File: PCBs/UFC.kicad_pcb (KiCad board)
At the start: 2 copper layers, 63 parts, among them J3 Power, J5 Matrix, J7 Driver output 2, J9 Driver output 1, SW1 SW_SPST, SW10 SW_SPST, SW11 SW_SPST, SW12 SW_SPST, SW13 SW_SPST, SW14 SW_SPST, SW15 SW_SPST, SW16 SW_SPST, SW17 SW_SPST, SW2 SW_SPST, SW3 SW_SPST, SW4 SW_SPST, SW5 SW_SPST, SW6 SW_SPST, SW7 SW_SPST, SW8 SW_SPST, SW9 SW_SPST

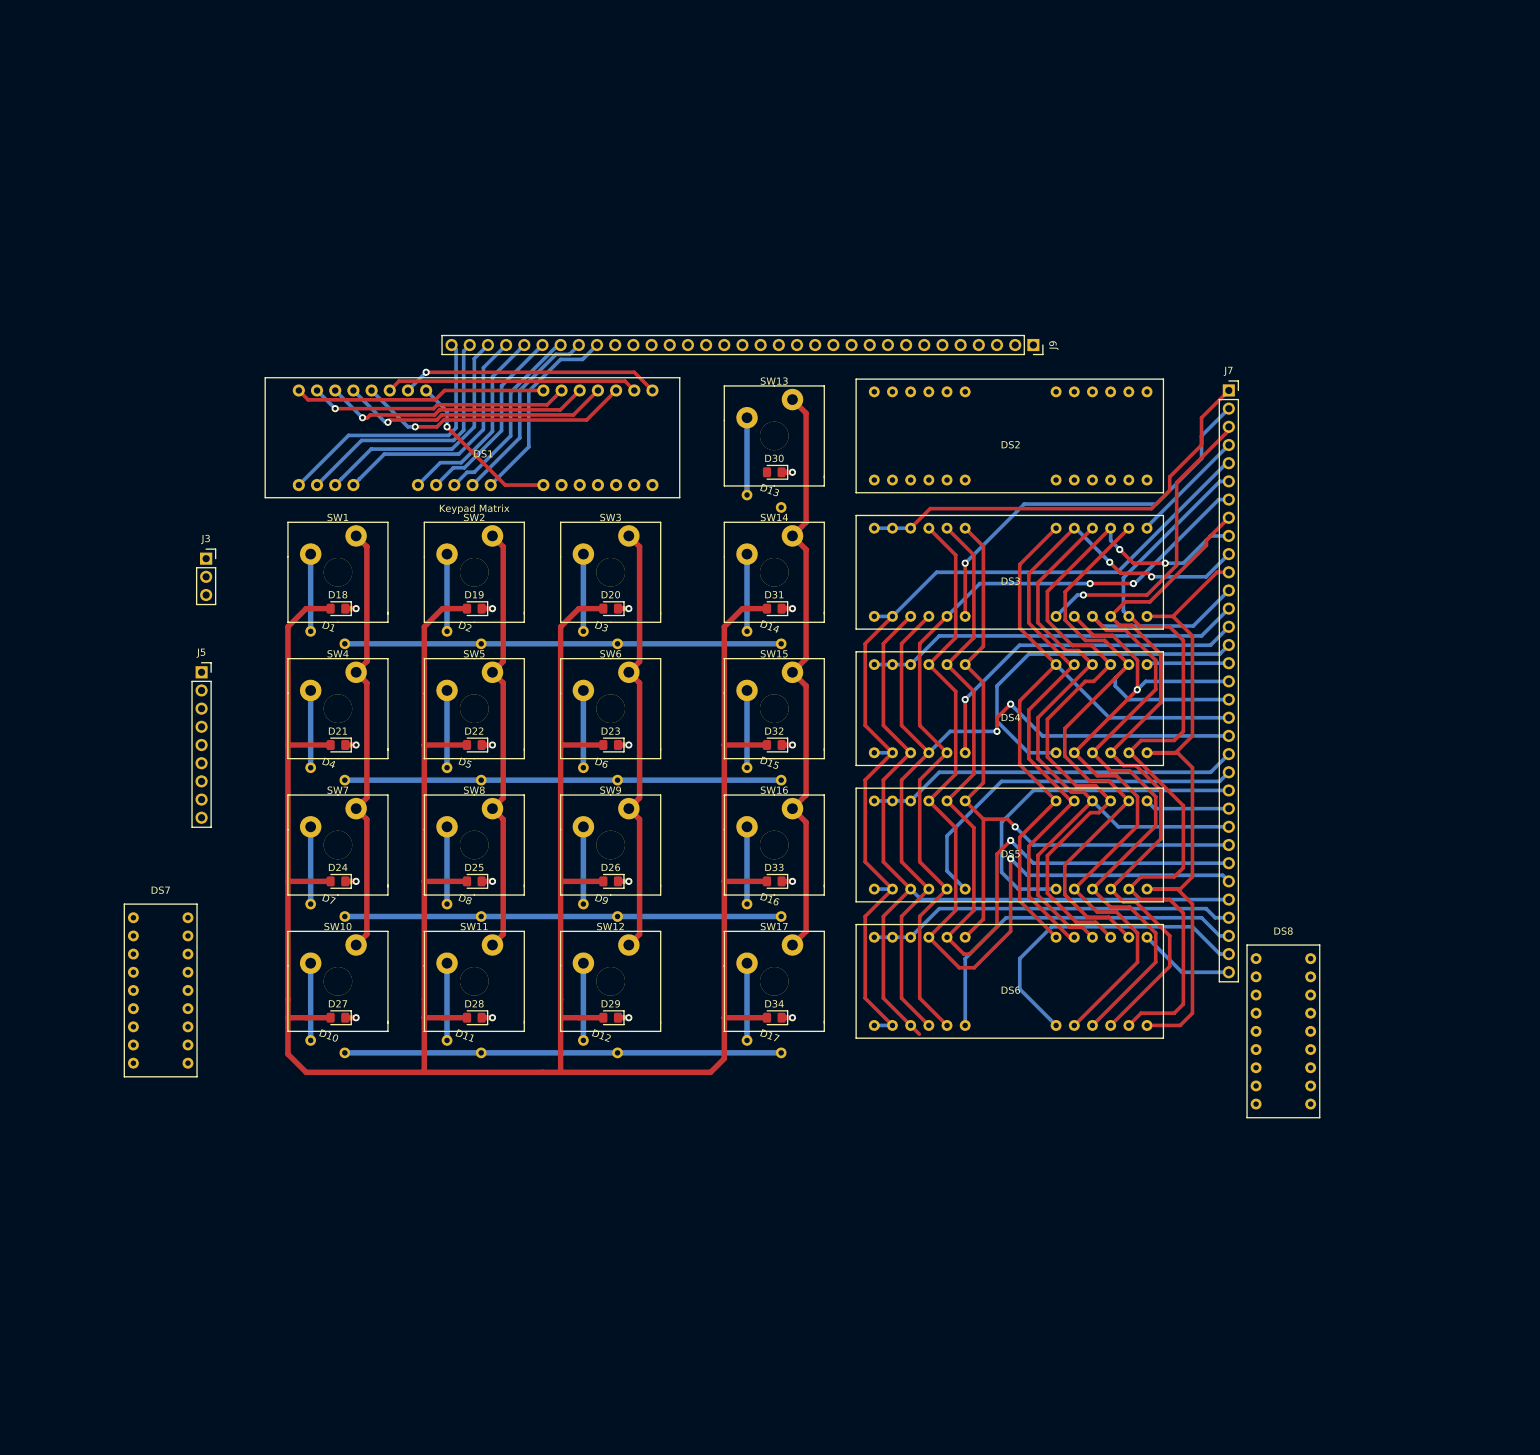
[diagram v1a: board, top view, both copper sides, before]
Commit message: Finished routing, updated comm channel displays
Decided to use (and again modify) open hornet's com channel indicators. Finished routing traces and adding ground planes on the main board, though it may be a little sloppy. Began work on the back side board, which will have the LED drivers and STM32. Re added the shift register board for now for the sake of having more pins.
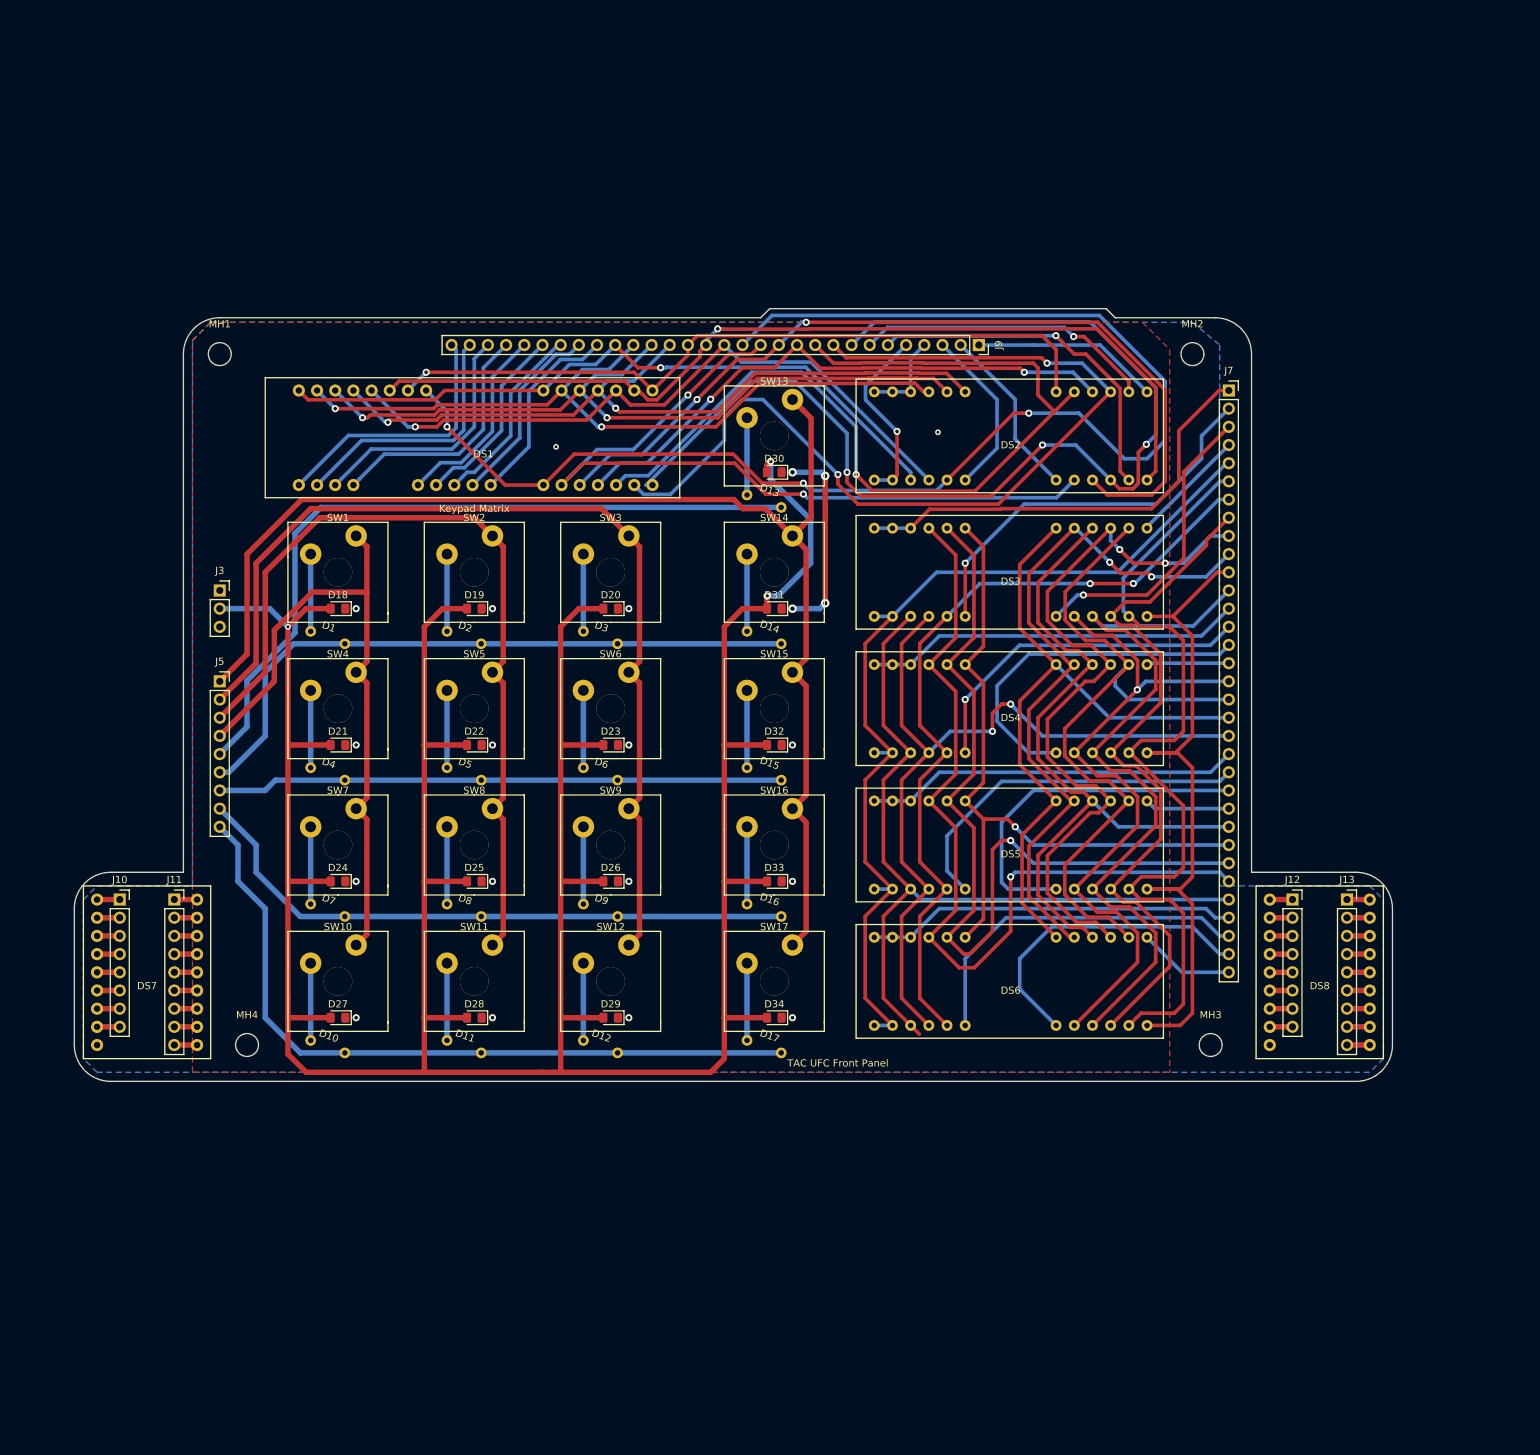
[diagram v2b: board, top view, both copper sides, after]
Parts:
- added J10: Conn_01x08_Male, Connector_PinSocket_2.54mm:PinSocket_1x08_P2.54mm_Vertical, F.Cu at (61.0, 128.3)
- added J11: Conn_01x09_Male, Connector_PinSocket_2.54mm:PinSocket_1x09_P2.54mm_Vertical, F.Cu at (68.6, 128.3)
- added J12: Conn_01x08_Male, Connector_PinSocket_2.54mm:PinSocket_1x08_P2.54mm_Vertical, F.Cu at (224.8, 128.3)
- added J13: Conn_01x09_Male, Connector_PinSocket_2.54mm:PinSocket_1x09_P2.54mm_Vertical, F.Cu at (232.4, 128.3)
- added MH1: MountingHole_3.2mm_M3, MountingHole:MountingHole_3.2mm_M3, F.Cu at (74.9, 52.1)
- added MH2: MountingHole_3.2mm_M3, MountingHole:MountingHole_3.2mm_M3, F.Cu at (210.8, 52.1)
- added MH3: MountingHole_3.2mm_M3, MountingHole:MountingHole_3.2mm_M3, F.Cu at (213.4, 148.6)
- added MH4: MountingHole_3.2mm_M3, MountingHole:MountingHole_3.2mm_M3, F.Cu at (78.7, 148.6)
- DS7, DS8: value 14SegDisplayLumex -> CommDS; footprint UFC:LDS-F3902RI -> UFC:OHComm
- J9: value Driver output 1 -> Conn_01x30_Male; footprint Connector_PinSocket_2.54mm:PinSocket_1x33_P2.54mm_Vertical -> Connector_PinSocket_2.54mm:PinSocket_1x30_P2.54mm_Vertical
- moved DS7 10.3 mm to (64.8, 138.4)
- moved J9 7.62 mm to (181.0, 50.8)
- moved DS8 6.75 mm to (228.6, 138.4)
- moved J3 4.84 mm to (74.9, 85.1)
- moved J5 2.84 mm to (74.9, 97.8)
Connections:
- DS1 pad 26: /J2 -> /J1
- DS1 pad 27: /K2 -> /K1
- DS1 pad 28: /L2 -> /L1
- DS1 pad 29: /M2 -> /M1
- DS1 pad 30: /N2 -> /N1
- DS1 pad 31: /P2 -> /P1
- DS7 pad 1: /J1 -> /COM13-1
- DS7 pad 10: /L1 -> /J1
- DS7 pad 11: /C1 -> /K1
- DS7 pad 12: /DP1 -> /L1
- DS7 pad 13: /COM13-1 -> /M1
- DS7 pad 14: /G1 -> /N1
- DS7 pad 15: /B1 -> /P1
- DS7 pad 16: /K1 -> /Q1
- DS7 pad 17: /COM13-1 -> /DP1
- DS7 pad 18: /A1 -> Net-(DS7-Pad18)
- DS7 pad 2: /H1 -> /A1
- DS7 pad 3: /F1 -> /B1
- DS7 pad 4: /COM13-1 -> /C1
- DS7 pad 5: /P1 -> /D1
- DS7 pad 7: /N1 -> /F1
- DS7 pad 8: /D1 -> /G1
- DS7 pad 9: /M1 -> /H1
- DS8 pad 1: /J1 -> /COM14-1
- DS8 pad 10: /L1 -> /J1
- DS8 pad 11: /C1 -> /K1
- DS8 pad 12: /DP1 -> /L1
- DS8 pad 13: /COM14-1 -> /M1
- DS8 pad 14: /G1 -> /N1
- DS8 pad 15: /B1 -> /P1
- DS8 pad 16: /K1 -> /Q1
- DS8 pad 17: /COM14-1 -> /DP1
- DS8 pad 18: /A1 -> Net-(DS8-Pad18)
- DS8 pad 2: /H1 -> /A1
- DS8 pad 3: /F1 -> /B1
- DS8 pad 4: /COM14-1 -> /C1
- DS8 pad 5: /P1 -> /D1
- DS8 pad 7: /N1 -> /F1
- DS8 pad 8: /D1 -> /G1
- DS8 pad 9: /M1 -> /H1
- J9 pad 1: /A1 -> /COM12-1
- J9 pad 10: /K1 -> /M1
- J9 pad 12: /M1 -> /K1
- J9 pad 13: /N1 -> /J1
- J9 pad 14: /P1 -> /H1
- J9 pad 15: /Q1 -> /E1
- J9 pad 16: /DP1 -> /F1
- J9 pad 17: /DOT1 -> /G1
- J9 pad 18: /COM15-1 -> /D1
- J9 pad 19: /COM14-1 -> /C1
- J9 pad 2: /B1 -> /COM11-1
- J9 pad 20: /COM13-1 -> /B1
- J9 pad 21: /COM12-1 -> /A1
- J9 pad 22: /COM11-1 -> /COM8-1
- J9 pad 23: /COM10-1 -> /COM7-1
- J9 pad 24: /COM9-1 -> /COM6-1
- J9 pad 25: /COM8-1 -> /COM5-1
- J9 pad 26: /COM7-1 -> /COM4-1
- J9 pad 27: /COM6-1 -> /COM3-1
- J9 pad 28: /COM5-1 -> /COM2-1
- J9 pad 29: /COM4-1 -> /COM1-1
- J9 pad 3: /C1 -> /COM10-1
- J9 pad 30: /COM3-1 -> /COM0-1
- J9 pad 4: /D1 -> /COM9-1
- J9 pad 5: /E1 -> /DOT1
- J9 pad 6: /F1 -> /DP1
- J9 pad 7: /G1 -> /Q1
- J9 pad 8: /H1 -> /P1
- J9 pad 9: /J1 -> /N1
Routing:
- net /H1: track 23.1 -> 201.2 mm, vias 1 -> 3
- net /P1: track 0.00 -> 160.5 mm, vias 0 -> 3
- net /N1: track 0.00 -> 135.6 mm, vias 0 -> 2
- net /M1: track 0.00 -> 133.0 mm, vias 0 -> 1
- net /K1: track 0.00 -> 126.1 mm, vias 0 -> 2
- net /J1: track 0.00 -> 118.2 mm, vias 0 -> 2
- net /ROW0: track 0.00 -> 104.6 mm
- net /F1: track 35.2 -> 136.8 mm, vias 0 -> 1
- net /COL4: track 82.5 -> 183.9 mm
- net /L1: track 0.00 -> 86.3 mm, vias 0 -> 2
- net /COL3: track 60.9 -> 138.8 mm
- net /B1: track 36.3 -> 111.7 mm, vias 1 -> 2
- net /C1: track 37.3 -> 112.3 mm, vias 1 -> 2
- net /D1: track 37.8 -> 112.8 mm, vias 1 -> 2
- net /G1: track 36.3 -> 109.7 mm
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- added copper zone on B.Cu, net /GND
- added copper zone on F.Cu, net /GND
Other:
- board outline added: 184.1 x 108 mm
- board text added: "TAC UFC Front Panel"

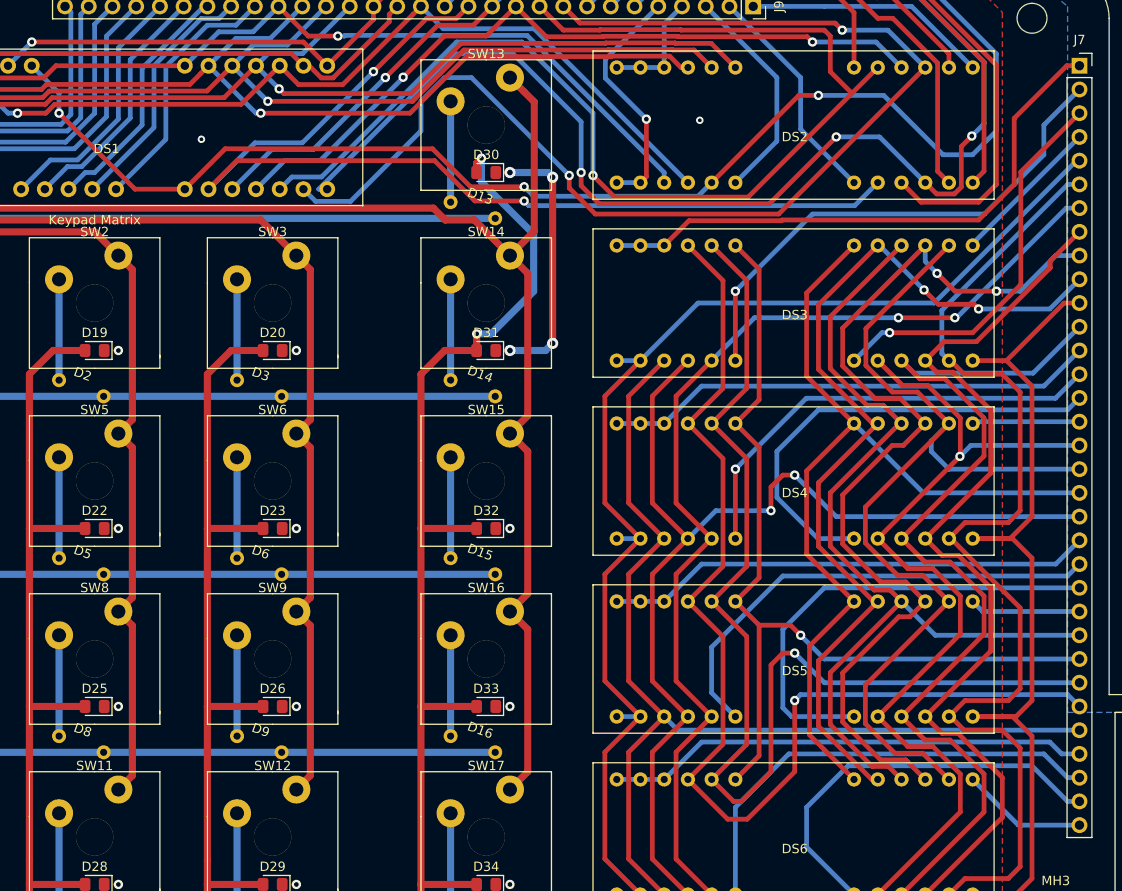
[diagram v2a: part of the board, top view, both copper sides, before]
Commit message: Updated silkscreen, fixed minor issues
Updated silkscreen to include pin designations, and fixed minor issue with ground plane
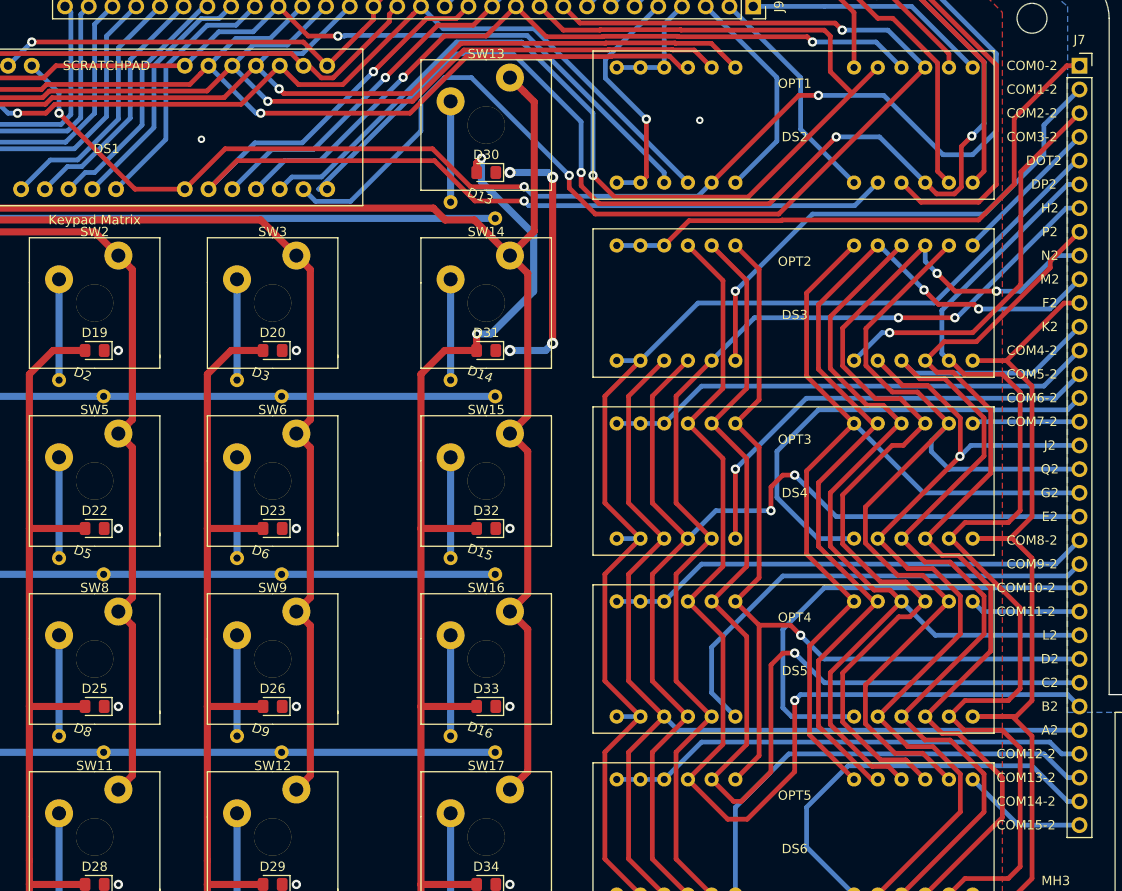
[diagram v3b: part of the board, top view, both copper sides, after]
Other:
- board text added: "A1"
- board text added: "A2"
- board text added: "B1"
- board text added: "B2"
- board text added: "C1"
- board text added: "C2"
- board text added: "CC-BY-NC-SA"
- board text added: "COM0-1"
- board text added: "COM0-2"
- board text added: "COM1-2"
- board text added: "COM10-2"
- board text added: "COM11-2"
- board text added: "COM12-1"
- board text added: "COM12-2"
- board text added: "COM13-2"
- board text added: "COM14-2"
- board text added: "COM15-2"
- board text added: "COM2-2"
- board text added: "COM3-2"
- board text added: "COM4-2"
- board text added: "COM5-2"
- board text added: "COM6-2"
- board text added: "COM7-2"
- board text added: "COM8-1"
- board text added: "COM8-2"
- board text added: "COM9-1"
- board text added: "COM9-2"
- board text added: "D1"
- board text added: "D2"
- board text added: "DOT1"
- board text added: "DOT2"
- board text added: "DP1"
- board text added: "DP2"
- board text added: "E1"
- board text added: "E2"
- board text added: "F1"
- board text added: "F2"
- board text added: "G1"
- board text added: "G2"
- board text added: "H1"
- board text added: "H2"
- board text added: "J1"
- board text added: "J2"
- board text added: "K1"
- board text added: "K2"
- board text added: "L1"
- board text added: "L2"
- board text added: "M1"
- board text added: "M2"
- board text added: "N1"
- board text added: "N2"
- board text added: "OPT1"
- board text added: "OPT2"
- board text added: "OPT3"
- board text added: "OPT4"
- board text added: "OPT5"
- board text added: "P1"
- board text added: "P2"
- board text added: "Q1"
- board text added: "Q2"
- board text added: "SCRATCHPAD"
